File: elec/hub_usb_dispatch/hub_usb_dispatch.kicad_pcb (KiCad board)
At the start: 2 copper layers, 88 x 70 mm, 63 parts, among them IC1 TS2596CM550_RNG, J1 USB_B_Mini, J10 Conn_01x02, J11 Emergency Stop, J12 Switch Logic, J13 BAT_POWER Display, J14 BAT_LOGIC Display, J15 Conn_01x02, J16 Conn_01x02, J17 Conn_01x02, J2 USB_A_Stacked_Double, J3 Conn_01x02, J4 Conn_01x02, J5 USB_A, J6 USB_A_Stacked_Double, J7 USB_A_Stacked_Double, J8 Conn_01x02, J9 Conn_01x02, U1 MIC5504-3.3YM5, U2 USB2517, Y1 24M

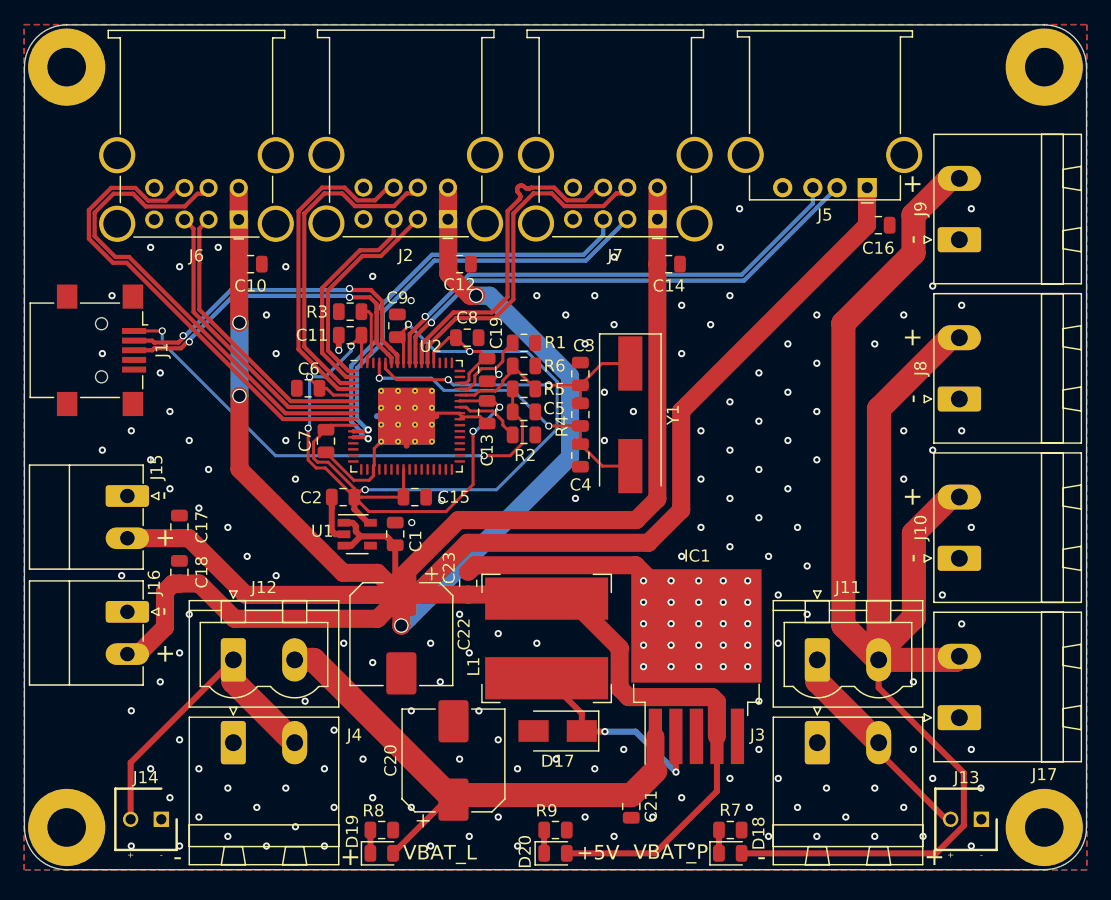
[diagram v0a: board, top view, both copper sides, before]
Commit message: ESD protection on data lines
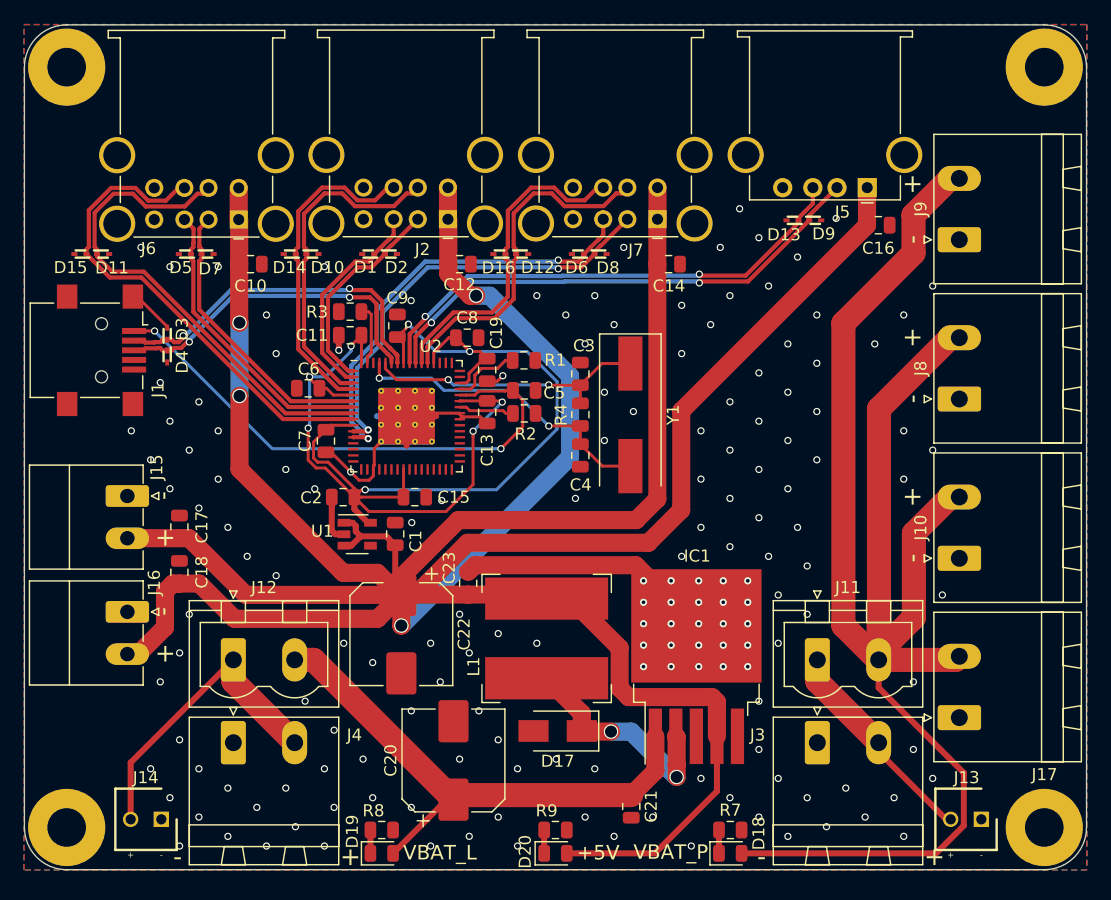
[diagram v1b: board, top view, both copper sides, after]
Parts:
- removed R5, R6: 100k, Resistor_SMD:R_0805_2012Metric
- added D1: ESD9B3.3ST5G, villanut_lib:ESD9B3.3ST5G, F.Cu at (78.5, 69.0)
- added D10: ESD9B3.3ST5G, villanut_lib:ESD9B3.3ST5G, F.Cu at (73.9, 69.0)
- added D11: ESD9B3.3ST5G, villanut_lib:ESD9B3.3ST5G, F.Cu at (56.5, 69.0)
- added D12: ESD9B3.3ST5G, villanut_lib:ESD9B3.3ST5G, F.Cu at (91.2, 69.0)
- added D13: ESD9B3.3ST5G, villanut_lib:ESD9B3.3ST5G, F.Cu at (113.6, 66.2)
- added D14: ESD9B3.3ST5G, villanut_lib:ESD9B3.3ST5G, F.Cu at (72.0, 69.0)
- added D15: ESD9B3.3ST5G, villanut_lib:ESD9B3.3ST5G, F.Cu at (54.6, 69.0)
- added D16: ESD9B3.3ST5G, villanut_lib:ESD9B3.3ST5G, F.Cu at (89.4, 69.0)
- added D2: ESD9B3.3ST5G, villanut_lib:ESD9B3.3ST5G, F.Cu at (80.4, 69.0)
- added D3: ESD9B3.3ST5G, villanut_lib:ESD9B3.3ST5G, F.Cu at (61.8, 75.6)
- added D4: ESD9B3.3ST5G, villanut_lib:ESD9B3.3ST5G, F.Cu at (61.8, 77.5)
- added D5: ESD9B3.3ST5G, villanut_lib:ESD9B3.3ST5G, F.Cu at (63.3, 69.0)
- added D6: ESD9B3.3ST5G, villanut_lib:ESD9B3.3ST5G, F.Cu at (95.9, 69.0)
- added D7: ESD9B3.3ST5G, villanut_lib:ESD9B3.3ST5G, F.Cu at (65.2, 69.0)
- added D8: ESD9B3.3ST5G, villanut_lib:ESD9B3.3ST5G, F.Cu at (97.7, 69.0)
- added D9: ESD9B3.3ST5G, villanut_lib:ESD9B3.3ST5G, F.Cu at (115.5, 66.2)
- C3, C4: value 18pF -> 33pF
- moved C5 1.78 mm to (91.4, 80.3)
- moved R2 1.78 mm to (91.4, 82.2)
- moved R1 1.45 mm to (91.4, 77.8)
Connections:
- U2 pad 44: Net-(R5-Pad1) -> Net-(C5-Pad1)
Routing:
- net Net-(R5-Pad1): track 8.45 -> 0.00 mm
- net GND: track 56.0 -> 60.2 mm, vias 178 -> 167
- net Net-(C5-Pad1): track 42.3 -> 44.9 mm
- net /4_D+: track 40.0 -> 41.1 mm
- net /6_D+: track 28.1 -> 27.2 mm
- net Net-(R2-Pad1): track 5.53 -> 4.62 mm
- net Net-(R1-Pad1): track 6.74 -> 5.84 mm
- net /4_D-: track 40.6 -> 41.5 mm
- net Net-(D17-Pad1): track 17.8 -> 18.4 mm
- net /7_D+: track 41.7 -> 42.0 mm, vias 1 -> 2
- net /7_D-: track 42.3 -> 42.7 mm, vias 1 -> 2
- net /5_D-: track 35.8 -> 36.0 mm, vias 1 -> 2
- net /5_D+: track 36.2 -> 36.4 mm, vias 1 -> 2

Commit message: V2.0 : fix dumb mistakes (capacitors pin 25 and 62, lower capacitance ESD diodes, RESET_N R-C, CFG_SEL2 and VBUS_DET resistor divider)
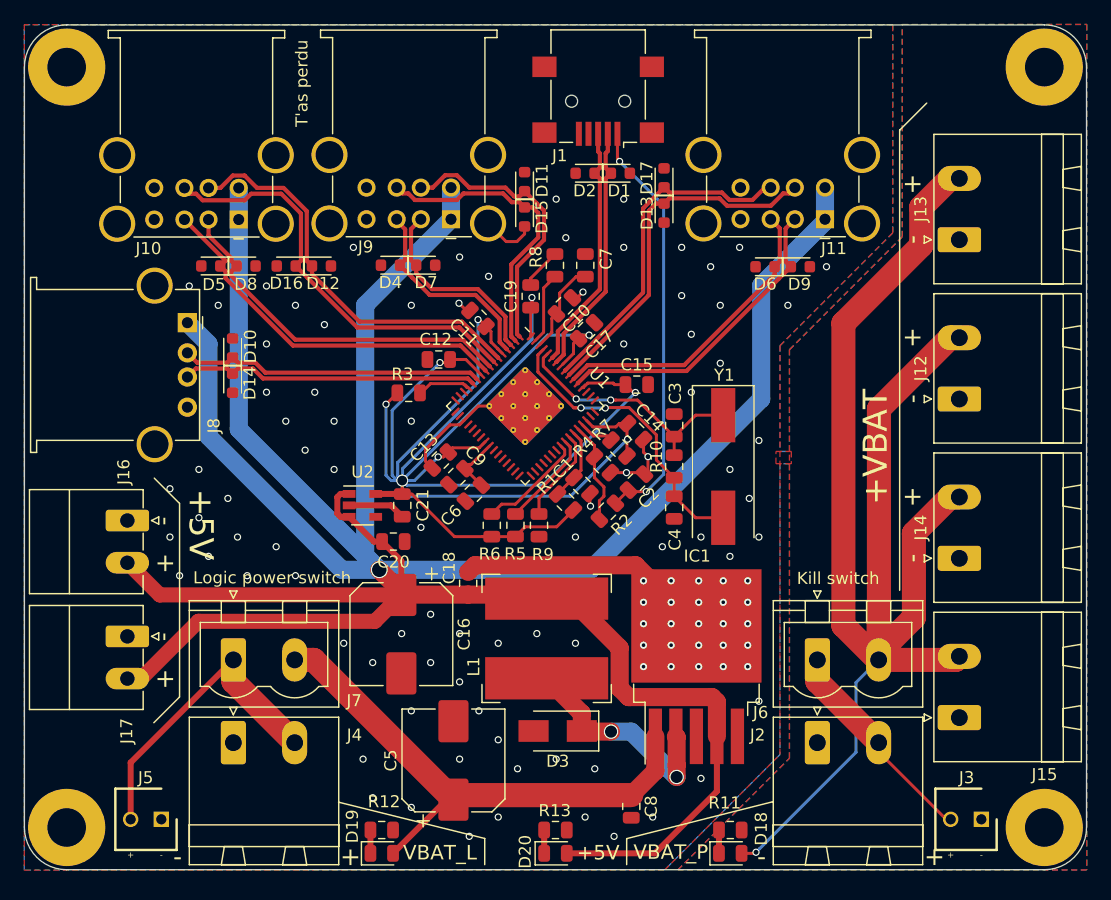
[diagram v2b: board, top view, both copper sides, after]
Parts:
- removed the C16 at (120.8, 66.6)
- removed the C18 at (62.8, 95.4)
- removed the C5 at (91.4, 80.3)
- removed the C8 at (86.7, 75.9)
- removed the D3 at (61.8, 75.6)
- removed the U1 at (77.6, 92.2)
- added C20: 1uF, Capacitor_SMD:C_0805_2012Metric, F.Cu at (80.6, 92.8)
- added C21: 1uF, Capacitor_SMD:C_0805_2012Metric, F.Cu at (81.3, 89.8)
- added D17: CG0603MLC-3.3LEA, Diode_SMD:D_0603_1608Metric, F.Cu at (103.0, 62.7)
- added R10: 1M, Resistor_SMD:R_0805_2012Metric, F.Cu at (103.8, 86.6)
- added R5: 10k, Resistor_SMD:R_0805_2012Metric, F.Cu at (90.7, 91.5)
- added R6: 10k, Resistor_SMD:R_0805_2012Metric, F.Cu at (88.7, 91.5)
- added R7: 10k, Resistor_SMD:R_0805_2012Metric, F.Cu at (99.3, 85.1)
- added R8: 12k, Resistor_SMD:R_0805_2012Metric, F.Cu at (94.0, 69.9)
- added R9: 10k, Resistor_SMD:R_0805_2012Metric, F.Cu at (92.6, 91.5)
- added U2: MIC5504-3.3YM5, Package_TO_SOT_SMD:SOT-23-5, F.Cu at (78.0, 89.8)
- C1: value 1uF -> 100nF
- C10, C12, C14, C17: value 4.7uF -> 100nF
- C6, C7: value 100nF -> 1uF
- D1, D10, D11, D12, D13, D14, D15, D16, D2, D4, D5, D6, D7, D8, D9: value ESD9B3.3ST5G -> CG0603MLC-3.3LEA; footprint villanut_lib:ESD9B3.3ST5G -> Diode_SMD:D_0603_1608Metric
- R1, R2: value 56k -> 100k
- R3: value 12k -> 10k
- R4: value 1M -> 100k
- moved J8 57.4 mm to (63.5, 74.7), turned to 270 degrees
- moved J1 46.0 mm to (97.5, 56.3), turned to 180 degrees
- moved C17 37.4 mm to (96.6, 75.3), turned to 45 degrees
- moved D15 36.9 mm to (91.4, 65.9), turned to 270 degrees
- moved D11 35.4 mm to (91.4, 63.0), turned to 90 degrees
- moved D8 29.4 mm to (68.4, 70.0)
- moved C10 26.2 mm to (94.7, 73.3), turned to 45 degrees
- moved C7 26.0 mm to (96.5, 69.9), turned to 90 degrees
- moved C2 24.3 mm to (100.7, 87.9), turned to 45 degrees
- moved D1 21.9 mm to (99.4, 62.3), turned to 0 degrees
- moved C15 20.6 mm to (100.7, 79.8)
- moved D4 20.0 mm to (80.3, 69.9), turned to 180 degrees
- moved D7 18.1 mm to (83.2, 69.9)
- moved D16 17.7 mm to (71.7, 70.0)
- moved D2 17.4 mm to (96.5, 62.3), turned to 180 degrees
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- renumbered C22 to C16, C23 to C18, C20 to C5, C21 to C8, D17 to D3, J6 to J10, J7 to J11, J8 to J12, J9 to J13, J10 to J14, J17 to J15, J15 to J16, J16 to J17, J3 to J2, J13 to J3, J14 to J5, J11 to J6, J12 to J7, J5 to J8, J2 to J9, R7 to R11, R8 to R12, R9 to R13, U2 to U1
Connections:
- C1 pad 1: +5V -> /RESET_N
- C10 pad 1: +5V -> Net-(C10-Pad1)
- C12 pad 1: +5V -> +3V3
- C14 pad 1: +5V -> +3V3
- C17 pad 1: +5V -> +3V3
- C2 pad 1: +3V3 -> Net-(C2-Pad1)
- C6 pad 1: +3V3 -> Net-(C6-Pad1)
- C7 pad 1: +3V3 -> Net-(C10-Pad1)
- C9 pad 1: +3V3 -> Net-(C6-Pad1)
- D1 pad 1: /1_D+ -> /D-
- D10 pad 1: /2_D- -> /5_D-
- D11 pad 1: /4_D- -> /1_D-
- D12 pad 1: /6_D- -> /3_D-
- D13 pad 1: /7_D+ -> /7_D-
- D14 pad 1: /2_D+ -> /5_D+
- D15 pad 1: /4_D+ -> /1_D+
- D16 pad 1: /6_D+ -> /3_D+
- D2 pad 1: /1_D- -> /D+
- D4 pad 1: /D+ -> /2_D+
- D5 pad 1: /3_D+ -> /4_D+
- D6 pad 1: /5_D+ -> /6_D+
- D7 pad 1: /3_D- -> /2_D-
- D8 pad 1: /5_D- -> /4_D-
- D9 pad 1: /7_D- -> /6_D-
- J1 pad 1: Net-(C5-Pad1) -> Net-(C2-Pad1)
- J10 pad 2: /3_D- -> /4_D-
- J10 pad 3: /3_D+ -> /4_D+
- J10 pad 6: /4_D- -> /3_D-
- J10 pad 7: /4_D+ -> /3_D+
- J11 pad 2: /5_D- -> /6_D-
- J11 pad 3: /5_D+ -> /6_D+
- J11 pad 6: /6_D- -> /7_D-
- J11 pad 7: /6_D+ -> /7_D+
- J8 pad 2: /7_D- -> /5_D-
- J8 pad 3: /7_D+ -> /5_D+
- J9 pad 2: /1_D- -> /2_D-
- J9 pad 3: /1_D+ -> /2_D+
- J9 pad 6: /2_D- -> /1_D-
- J9 pad 7: /2_D+ -> /1_D+
- R1 pad 1: Net-(R1-Pad1) -> /RESET_N
- R1 pad 2: GND -> +3V3
- R2 pad 1: Net-(R2-Pad1) -> /VBUS_DET
- R2 pad 2: GND -> Net-(C2-Pad1)
- R3 pad 1: Net-(R3-Pad1) -> +3V3
- R3 pad 2: GND -> Net-(R3-Pad2)
- R4 pad 1: Net-(C3-Pad1) -> GND
- R4 pad 2: Net-(C4-Pad1) -> /VBUS_DET
- U1 pad 13: Net-(U2-Pad13) -> Net-(R3-Pad2)
- U1 pad 25: Net-(U2-Pad25) -> Net-(C6-Pad1)
- U1 pad 40: GND -> Net-(R6-Pad2)
- U1 pad 41: GND -> Net-(R5-Pad2)
- U1 pad 42: Net-(R2-Pad1) -> Net-(R9-Pad1)
- U1 pad 43: +3V3 -> /RESET_N
- U1 pad 44: Net-(C5-Pad1) -> /VBUS_DET
- U1 pad 45: Net-(R1-Pad1) -> Net-(R7-Pad2)
- U1 pad 62: Net-(U2-Pad62) -> Net-(C10-Pad1)
- U1 pad 63: Net-(R3-Pad1) -> Net-(R8-Pad1)
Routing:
- net +3V3: track 118.5 -> 175.5 mm, vias 8 -> 9
- net Net-(C5-Pad1): track 44.9 -> 0.00 mm, vias 2 -> 0
- net +5V: track 319.9 -> 275.8 mm, vias 4 -> 1
- net Net-(C2-Pad1): track 0.00 -> 34.9 mm, vias 0 -> 2
- net /VBAT_PWR: track 135.0 -> 120.4 mm, vias 0 -> 1
- net /7_D+: track 42.0 -> 28.3 mm, vias 2 -> 0
- net /7_D-: track 42.7 -> 29.7 mm, vias 2 -> 0
- net /5_D+: track 36.4 -> 24.8 mm, vias 2 -> 0
- net /2_D-: track 27.7 -> 16.4 mm
- net /4_D-: track 41.5 -> 30.3 mm
- net /5_D-: track 36.0 -> 25.2 mm, vias 2 -> 0
- net /3_D+: track 24.7 -> 35.2 mm
- net /2_D+: track 27.1 -> 17.1 mm
- net /4_D+: track 41.1 -> 31.3 mm
- net /3_D-: track 23.9 -> 33.5 mm
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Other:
- net class usb added: clearance 0.13, trace_width 0.25, via_dia 0.8, via_drill 0.4
- rule trace_min: 0.25 -> 0.1
- board text added: "+VBAT"
- board text added: "Dispatch V2.0"
- board text added: "Kill switch"
- board text added: "Logic power"
- board text added: "Logic power switch"
- board text added: "Power"
- board text added: "T'as perdu"
- board text removed: "Dispatch V1.0"
